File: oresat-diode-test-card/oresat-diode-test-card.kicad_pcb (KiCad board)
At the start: 4 copper layers, 99.8 x 94.6 mm, 140 parts, among them J6 J-SAMTEC-TFM-120-X1-XXX-D-RA, J7 ORESAT-DEBUG-CONNECTOR-ALL, Q1 DMP2240UDM, Q2 DMP3050LVT-7, Q3 NMOS, Q4 DMP3050LVT-7, Q7 MOSFET-PCH-SOT23-6, Q8 PMV45EN, Q9 PMV45EN, U1 TCAN330, U10 TPS62111RSA, U11 MIC842LYC5, U12 MIC842LYC5, U2 MAX7310, U3 TS5A21366DCUR, U4 TLV6001DCK, U501 TLV6001DCK, U6 MAX4211, U7 STM32F091C, U8 NX3L4051-Q100, U9 TLV6001DCK, X2 CRYSTAL-WITH-GND

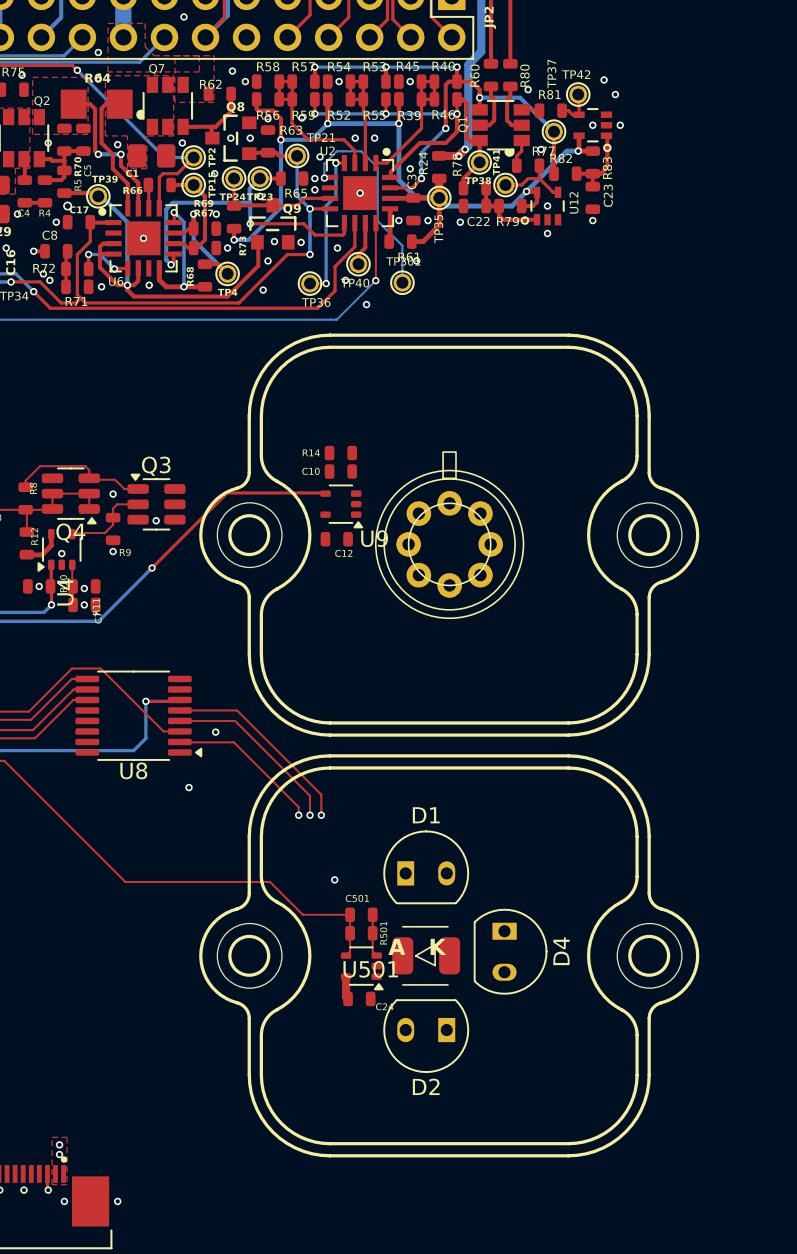
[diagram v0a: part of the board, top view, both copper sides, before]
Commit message: Clean up of EAGLE imported ICs, added build directory, moved and locked diode hats.
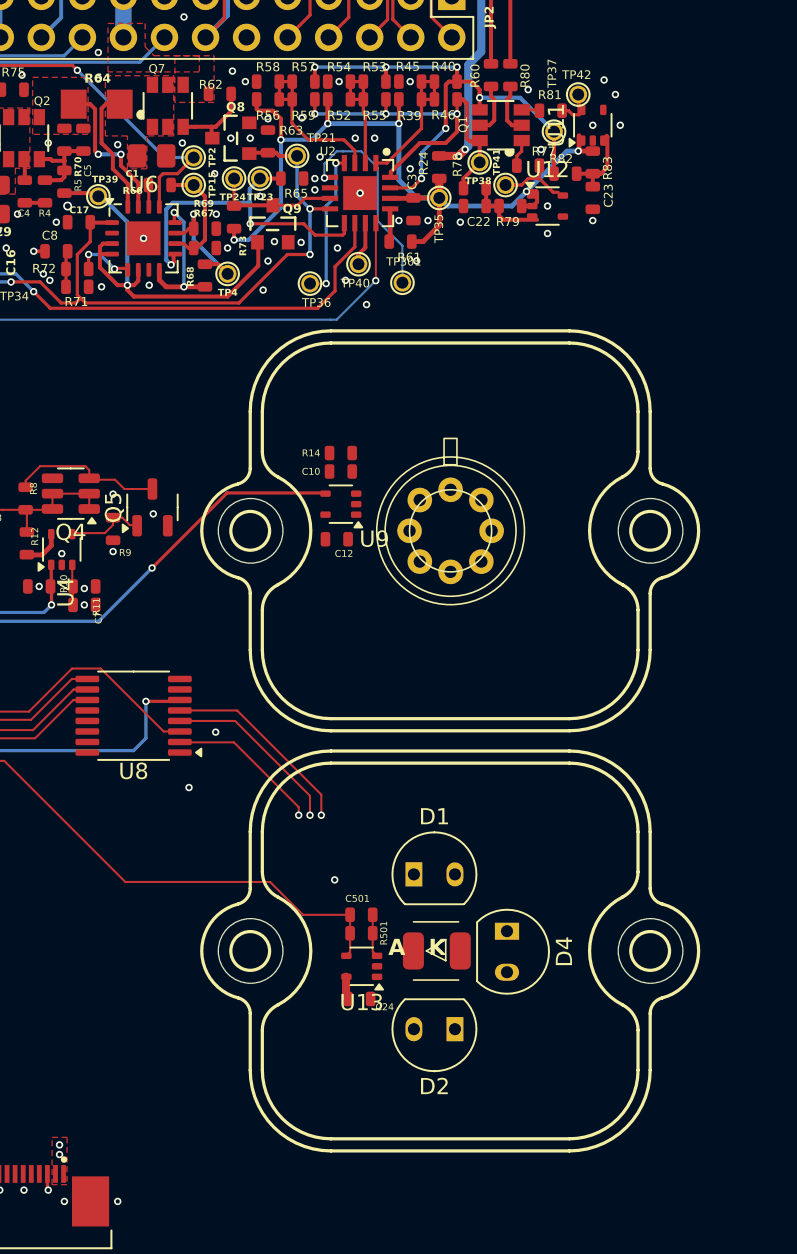
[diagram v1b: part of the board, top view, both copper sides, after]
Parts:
- removed Q3: NMOS, Package_TO_SOT_SMD:SOT-23-6
- removed U501: TLV6001DCK, Package_TO_SOT_SMD:SOT-353_SC-70-5
- added Q5: PMV45EN, Package_TO_SOT_SMD:SOT-23-3, F.Cu at (144.6, 102.5)
- added U13: TLV6001DCK, Package_TO_SOT_SMD:SOT-353_SC-70-5, F.Cu at (157.5, 130.9)
- U11, U12: footprint oresat-proto-card:SC70-5 -> Package_TO_SOT_SMD:SOT-353_SC-70-5
- U6: footprint oresat-proto-card:QFN65P400X400X80-17T210 -> Package_DFN_QFN:QFN-16-1EP_4x4mm_P0.65mm_EP2.1x2.1mm
- moved U5 0.84 mm to (163.0, 104.0)
- moved D8 0.72 mm to (163.0, 130.0)
- moved D1 0.51 mm to (160.7, 125.3)
- moved D2 0.51 mm to (163.3, 134.8)
- moved REF** 0.31 mm to (163.0, 130.0)
- moved REF** 0.27 mm to (163.0, 104.0)
- moved D4 0.15 mm to (166.5, 128.8)
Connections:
- U11 pad 3: (no net) -> unconnected-(U11-Pad3)
- U12 pad 3: (no net) -> unconnected-(U12-Pad3)
- U6 pad 2: (no net) -> unconnected-(U6-NC-Pad2)
- U8 pad 7: (no net) -> unconnected-(U8-Pad7)
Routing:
- net Net-(Q4-G): track 8.62 -> 9.51 mm
- net Net-(Q5-G): track 5.43 -> 4.90 mm
